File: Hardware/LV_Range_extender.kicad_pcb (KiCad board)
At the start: 2 copper layers, 25.5 x 13 mm, 18 parts, among them J1 Conn_01x03_Female, J2 Conn_01x03_Female, J3 Conn_01x04_Female, U1 ME6211A33M3G-N, U2 SN74LVC1T45DBV, U3 SN75176AD, U4 TS5A23159DGS

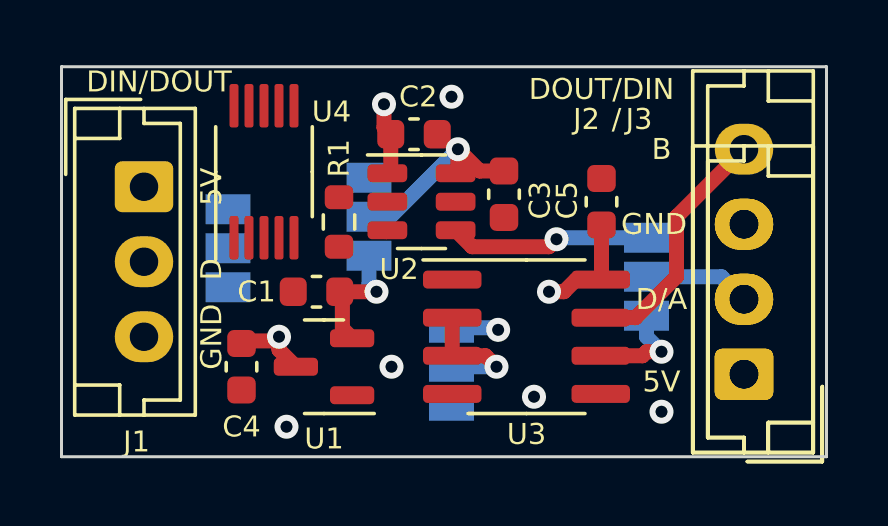
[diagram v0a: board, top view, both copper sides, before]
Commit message: add multiplexer
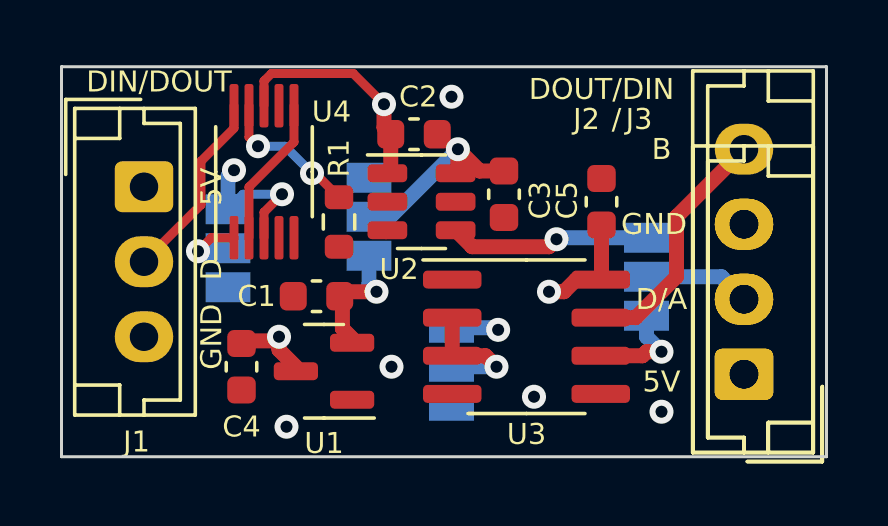
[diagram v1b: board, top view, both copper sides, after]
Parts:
- moved C1 0.15 mm to (133.2, 82.9)
- moved U1 0.15 mm to (133.5, 85.4)
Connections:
- J1 pad 2: DIN -> DIN/TTL
- JP4 pad 1: LV_IN -> GND
- JP4 pad 2: DIN -> MUX
- JP4 pad 3: TTL -> +5V
- U3 pad 1: unconnected-(U3-Pad1) -> Receiver
- U3 pad 4: TTL -> Driver
- U4 pad 1: unconnected-(U4-Pad1) -> MUX
- U4 pad 10: unconnected-(U4-Pad10) -> DIN/TTL
- U4 pad 2: unconnected-(U4-Pad2) -> Com
- U4 pad 3: unconnected-(U4-Pad3) -> GND
- U4 pad 4: unconnected-(U4-Pad4) -> Receiver
- U4 pad 5: unconnected-(U4-Pad5) -> MUX
- U4 pad 6: unconnected-(U4-Pad6) -> Com
- U4 pad 7: unconnected-(U4-Pad7) -> Driver
- U4 pad 8: unconnected-(U4-Pad8) -> +5V
- U4 pad 9: unconnected-(U4-Pad9) -> LV_IN
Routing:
- net DIN/TTL: track 0.00 -> 6.44 mm
- net +5V: track 8.62 -> 14.0 mm
- net GND: track 1.58 -> 6.67 mm, vias 6 -> 8
- net Com: track 0.00 -> 5.02 mm
- net LV_IN: track 0.00 -> 4.88 mm, vias 0 -> 2
- net MUX: track 0.00 -> 2.43 mm, vias 0 -> 1

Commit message: update multiplexing
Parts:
- removed JP2: SolderJumper_3_Open, Jumper:SolderJumper-3_P1.3mm_Open_Pad1.0x1.5mm
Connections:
- net MUX renamed Net-(U4-Pad1)
- C2 pad 1: +5V -> Net-(C2-Pad1)
- C3 pad 2: Net-(C3-Pad2) -> +5V
- J1 pad 2: DIN/TTL -> LV_A
- JP1 pad 1: LV -> DOUT/A
- JP1 pad 2: DOUT/A -> LV_B
- JP3 pad 2: Net-(C3-Pad2) -> Net-(C2-Pad1)
- R1 pad 1: LV_IN -> LV_A
- U2 pad 1: +5V -> Net-(C2-Pad1)
- U2 pad 4: LV -> LV_B
- U2 pad 6: Net-(C3-Pad2) -> +5V
- U3 pad 2: Net-(JP2-Pad2) -> RS_Enable
- U3 pad 3: Net-(JP2-Pad2) -> RS_Enable
- U4 pad 10: DIN/TTL -> RS_Enable
- U4 pad 2: Com -> GND
- U4 pad 6: Com -> RS
- U4 pad 9: LV_IN -> +5V
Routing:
- net RS_Enable: track 0.00 -> 10.8 mm, vias 0 -> 1
- net Net-(C2-Pad1): track 0.00 -> 7.79 mm
- net DOUT/A: track 3.56 -> 10.3 mm, vias 0 -> 1
- net LV: track 6.71 -> 0.00 mm, vias 1 -> 0
- net Net-(C3-Pad2): track 6.56 -> 0.00 mm, vias 1 -> 0
- net DIN/TTL: track 6.44 -> 0.00 mm
- net RS: track 3.49 -> 8.51 mm
- net Com: track 5.02 -> 0.00 mm
- net LV_IN: track 4.88 -> 0.00 mm, vias 2 -> 0
- net LV_A: track 0.00 -> 4.88 mm
- net Net-(JP2-Pad2): track 4.40 -> 0.00 mm, vias 1 -> 0
- net +5V: track 14.0 -> 12.7 mm, vias 3 -> 6

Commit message: Add ordered version V1
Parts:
- added JP2: SolderJumper_2_Open, Jumper:SolderJumper-2_P1.3mm_Open_Pad1.0x1.5mm, F.Cu at (144.2, 84.2)
- moved R1 5.08 mm to (138.7, 78.5), turned to 90 degrees
- moved C3 4.68 mm to (135.0, 80.8), turned to 0 degrees
- moved C2 3.86 mm to (138.5, 80.8)
- moved U2 1.73 mm to (135.8, 78.3), turned to 180 degrees
- moved U3 1.08 mm to (139.2, 84.5)
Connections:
- C2 pad 1: Net-(C2-Pad1) -> +5V
- C3 pad 2: +5V -> Net-(JP3-Pad2)
- J1 pad 2: LV_A -> LV_B
- JP1 pad 2: LV_B -> LV_A
- JP3 pad 2: Net-(C2-Pad1) -> Net-(JP3-Pad2)
- JP4 pad 2: Net-(U4-Pad1) -> MUX
- U2 pad 1: Net-(C2-Pad1) -> +5V
- U2 pad 5: GND -> MUX
- U2 pad 6: +5V -> Net-(JP3-Pad2)
- U3 pad 6: RS -> Net-(U3-Pad6)
- U4 pad 1: Net-(U4-Pad1) -> MUX
- U4 pad 5: Net-(U4-Pad1) -> MUX
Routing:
- net Driver: track 0.00 -> 18.6 mm, vias 0 -> 2
- net LV_B: track 0.00 -> 13.1 mm, vias 0 -> 1
- net MUX: track 0.00 -> 12.6 mm, vias 0 -> 1
- net RS: track 8.51 -> 18.4 mm
- net RS_Enable: track 10.8 -> 18.6 mm, vias 1 -> 2
- net Net-(C2-Pad1): track 7.79 -> 0.00 mm
- net Receiver: track 0.00 -> 7.49 mm
- net Net-(JP3-Pad2): track 0.00 -> 5.19 mm, vias 0 -> 1
- net DOUT/A: track 10.3 -> 7.63 mm, vias 1 -> 0
- net Net-(U3-Pad6): track 0.00 -> 2.64 mm
- net Net-(U4-Pad1): track 2.43 -> 0.00 mm, vias 1 -> 0
- net GND: track 6.67 -> 8.82 mm, vias 8 -> 7
- net LV_A: track 4.88 -> 6.85 mm, vias 0 -> 1
- net Net-(U2-Pad3): track 0.07 -> 1.90 mm
- net +3V3: track 4.13 -> 3.25 mm
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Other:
- board text added: "G"
- board text added: "LV"
- board text added: "MUX"
